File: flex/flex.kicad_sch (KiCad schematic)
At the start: 69 parts, among them J1 Conn_01x04_Female, J2 Conn_01x05_Female, J3 Conn_01x03_Female, J4 Conn_01x06_Female, J5 Conn_01x03_Female, SW10 SW_Push, SW11 SW_Push, SW12 SW_Push, SW15 SW_Push, SW16 SW_Push, SW17 SW_Push, SW20 SW_Push, SW21 SW_Push, SW22 SW_Push, SW24 SW_Push, SW25 SW_Push, SW26 SW_Push, SW6 SW_Push, SW7 SW_Push, SW8 SW_Push

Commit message: licenses
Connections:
- net Gnd: no longer D21.2 (VSS), D22.2 (VSS), D23.2 (VSS), D24.2 (VSS), D25.2 (VSS), D26.2 (VSS), D37.2 (VSS), D38.2 (VSS), D39.2 (VSS), D40.2 (VSS), D41.2 (VSS), D42.2 (VSS), D47.2 (VSS), D48.2 (VSS), D49.2 (VSS), D50.2 (VSS), D51.2 (VSS), D52.2 (VSS), D55.2 (VSS), D56.2 (VSS), D57.2 (VSS), D58.2 (VSS), D59.2 (VSS), D60.2 (VSS)
- net Vcc: no longer D21.4 (VDD), D22.4 (VDD), D23.4 (VDD), D24.4 (VDD), D25.4 (VDD), D26.4 (VDD), D33.4 (VDD), D37.4 (VDD), D38.4 (VDD), D39.4 (VDD), D40.4 (VDD), D41.4 (VDD), D42.4 (VDD), D47.4 (VDD), D48.4 (VDD), D49.4 (VDD), D5.4 (VDD), D50.4 (VDD), D51.4 (VDD), D52.4 (VDD), D55.4 (VDD), D56.4 (VDD), D57.4 (VDD), D58.4 (VDD), D59.4 (VDD), D60.4 (VDD), D7.4 (VDD)
- net at D21.3 (DIN), D22.3 (DIN), D33.1 (DOUT): no longer D34.1 (DOUT)
- net at D42.1 (DOUT), D48.3 (DIN): no longer D41.1 (DOUT), D47.3 (DIN)
- net at D5.3 (DIN), D6.3 (DIN): no longer R1.2, R2.2
- new net: D22.2 (VSS), D24.2 (VSS), D26.2 (VSS), D38.2 (VSS), D40.2 (VSS), D42.2 (VSS)
- new net: D22.4 (VDD), D24.4 (VDD), D26.4 (VDD), D38.4 (VDD), D40.4 (VDD), D42.4 (VDD)
- new net: D21.2 (VSS), D23.2 (VSS), D25.2 (VSS), D37.2 (VSS), D39.2 (VSS), D41.2 (VSS), D47.2 (VSS), D49.2 (VSS), D51.2 (VSS)
- new net: D21.4 (VDD), D23.4 (VDD), D25.4 (VDD), D37.4 (VDD), D39.4 (VDD), D41.4 (VDD)
- new net: D33.4 (VDD), D5.4 (VDD), D7.4 (VDD)
- new net: D48.2 (VSS), D50.2 (VSS), D52.2 (VSS), D56.2 (VSS), D58.2 (VSS), D60.2 (VSS)
- new net: D48.4 (VDD), D50.4 (VDD), D52.4 (VDD), D56.4 (VDD), D58.4 (VDD), D60.4 (VDD)
- new net: D41.1 (DOUT), D47.3 (DIN)
- new net: D47.4 (VDD), D49.4 (VDD), D51.4 (VDD), D55.4 (VDD), D57.4 (VDD), D59.4 (VDD)
- new net: D55.2 (VSS), D57.2 (VSS), D59.2 (VSS)
- new net: R1.2, R2.2
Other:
- note added: "Diodes and switches"
- note added: "MCU connector"
- note added: "RGB"
- note added: "RGB connectors"
- note added: "This work is licensed under a Creative Commons Attribution-NonCommercial-ShareAlike 4.0 International License."
- note added: "Thumb cluster connector"
- company: (none) -> bastard keyboards
- title: (none) -> flex.sch
- moved on the sheet: C1, C2, D11, D12, D13, D14, D15, D16, D17, D19, D20, D21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

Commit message: cleanup schem, reversible r and c
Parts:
- removed C2: C, Capacitor_SMD:C_1206_3216Metric_Pad1.42x1.75mm_HandSolder, symbol Device:C
- removed R2: R, Resistor_SMD:R_1206_3216Metric_Pad1.42x1.75mm_HandSolder, symbol Device:R
- added D1, D10, D28, D3, D30, D44, D46, D54, D62, D64, D66, D68, D70, D72, D74: RIGHT_D, custom:Diode_TH_SOD123, symbol Device:D
- added D18, D2, D29, D4, D43, D45, D53, D61, D63, D65, D67, D69, D71, D73, D75: LEFT_D, custom:Diode_TH_SOD123, symbol Device:D
- C1: value C -> NA_C; footprint Capacitor_SMD:C_1206_3216Metric_Pad1.42x1.75mm_HandSolder -> custom:C_1206_3216Metric_Pad1.33x1.80mm_HandSolder_reversible
- D11, D12, D13, D14, D15, D16, D17, D19, D20, D27, D31, D32, D35, D36, D9: value D -> NA_D
- R1: value R -> NA_R; footprint Resistor_SMD:R_1206_3216Metric_Pad1.42x1.75mm_HandSolder -> custom:R_1206_3216Metric_Pad1.30x1.75mm_HandSolder_reversible
- SW10, SW11, SW12, SW15, SW16, SW17, SW20, SW21, SW22, SW24, SW25, SW26, SW6, SW7, SW8: value SW_Push -> NA_SW_Push
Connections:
- net col2: now also D70.1 (K), D71.1 (K), D72.1 (K), D73.1 (K), D74.1 (K), D75.1 (K)
- net col3: now also D64.1 (K), D65.1 (K), D66.1 (K), D67.1 (K), D68.1 (K), D69.1 (K)
- net col4: now also D46.1 (K), D53.1 (K), D54.1 (K), D61.1 (K), D62.1 (K), D63.1 (K)
- net col5: now also D28.1 (K), D29.1 (K), D30.1 (K), D43.1 (K), D44.1 (K), D45.1 (K)
- net col6: now also D1.1 (K), D10.1 (K), D18.1 (K), D2.1 (K), D3.1 (K), D4.1 (K)
- net at D27.2 (A), SW16.2: now also D54.2 (A), D61.2 (A)
- net at D9.2 (A), SW6.2: now also D70.2 (A), D71.2 (A)
- net at D17.2 (A), SW12.2: now also D68.2 (A), D69.2 (A)
- net at D31.2 (A), SW22.2: now also D44.2 (A), D45.2 (A)
- net at D32.2 (A), SW21.2: now also D30.2 (A), D43.2 (A)
- net at D35.2 (A), SW26.2: now also D10.2 (A), D18.2 (A)
- net at D19.2 (A), SW11.2: now also D66.2 (A), D67.2 (A)
- net at D20.2 (A), SW17.2: now also D62.2 (A), D63.2 (A)
- net at D12.2 (A), SW8.2: now also D74.2 (A), D75.2 (A)
- net at D16.2 (A), SW24.2: now also D1.2 (A), D2.2 (A)
- net at D14.2 (A), SW20.2: now also D28.2 (A), D29.2 (A)
- net at D36.2 (A), SW25.2: now also D3.2 (A), D4.2 (A)
- net at D11.2 (A), SW10.2: now also D64.2 (A), D65.2 (A)
- net at D13.2 (A), SW15.2: now also D46.2 (A), D53.2 (A)
- net at D15.2 (A), SW7.2: now also D72.2 (A), D73.2 (A)
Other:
- moved on the sheet: C1, D11, D12, D13, D14, D15, D16, D17, D19, D20, D21, D22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

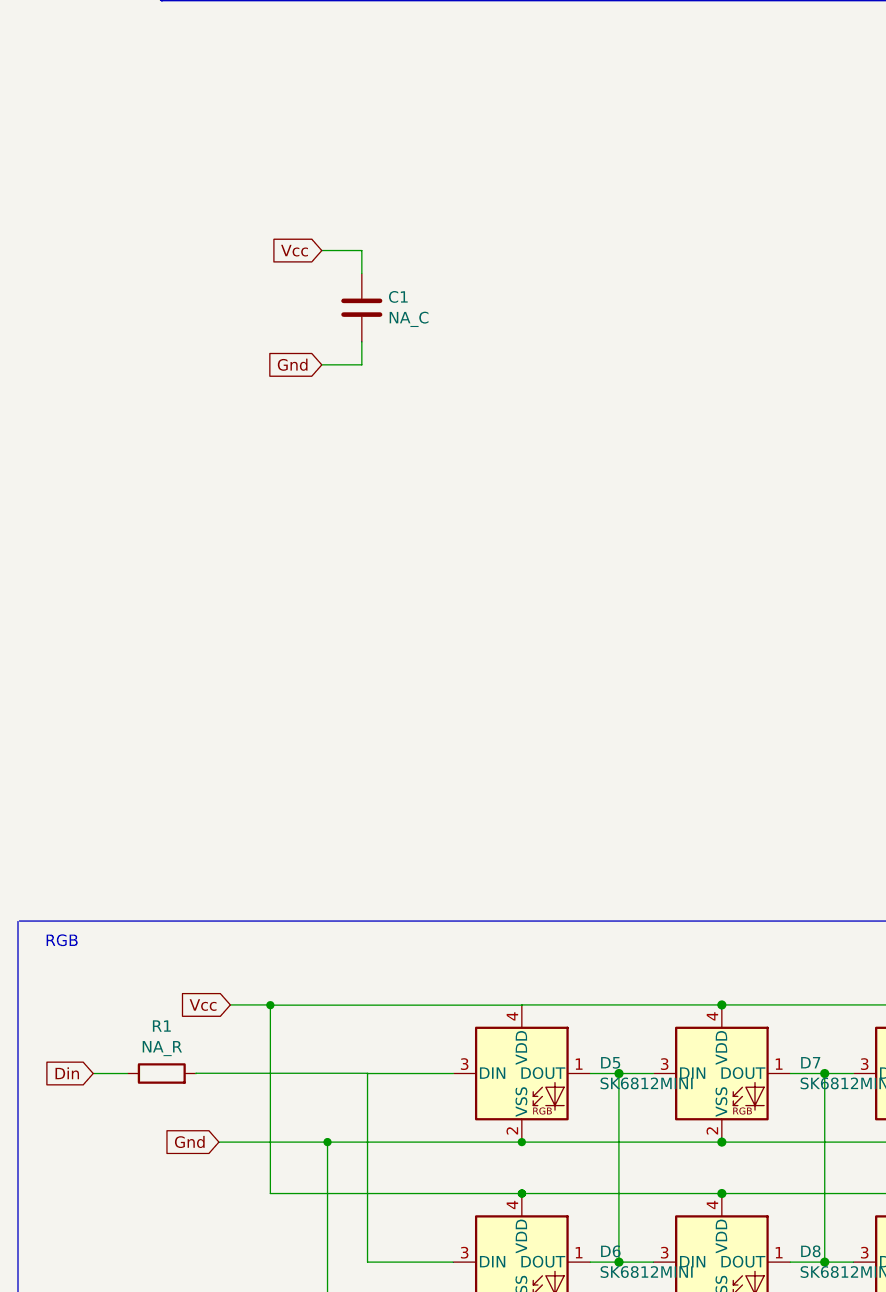
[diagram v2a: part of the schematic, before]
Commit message: place smd components
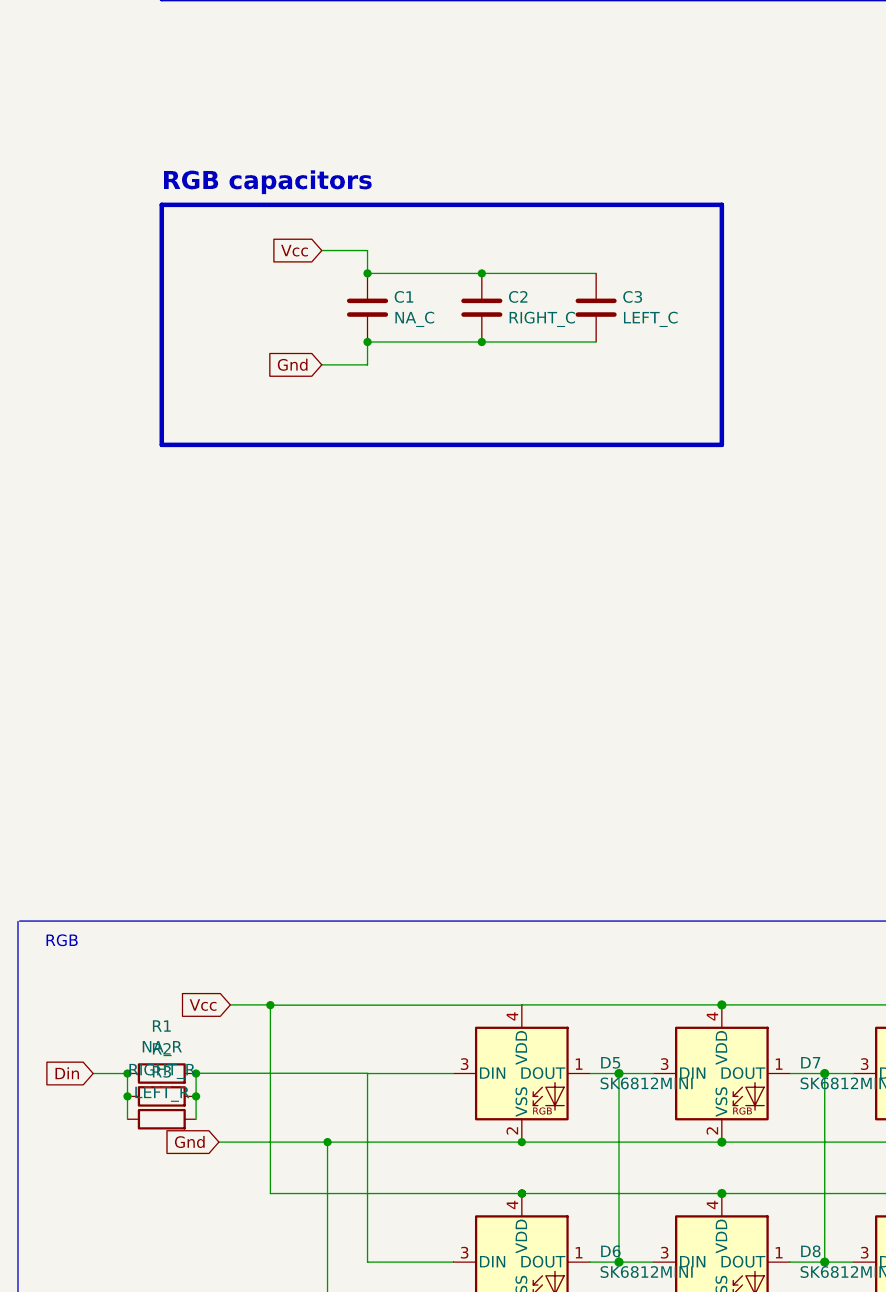
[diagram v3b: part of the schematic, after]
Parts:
- added C2: RIGHT_C, custom:R_0402, symbol Device:C
- added C3: LEFT_C, custom:R_0402, symbol Device:C
- added R2: RIGHT_R, custom:R_0402, symbol Device:R
- added R3: LEFT_R, custom:R_0402, symbol Device:R
- D1, D10, D18, D2, D28, D29, D3, D30, D4, D43, D44, D45, D46, D53, D54, D61, D62, D63, D64, D65, D66, D67, D68, D69, D70, D71, D72, D73, D74, D75: footprint custom:Diode_TH_SOD123 -> custom:D_SOD-523
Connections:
- net Din: now also R2.1, R3.1
- net Gnd: now also C2.2, C3.2
- net Vcc: now also C2.1, C3.1
- net at R1.2: now also R2.2, R3.2
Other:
- note added: "RGB capacitors"
- moved on the sheet: C1

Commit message: change LEDs
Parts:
- D21, D23, D25, D33, D37, D39, D41, D47, D49, D5, D51, D55, D57, D59, D7: value SK6812MINI -> RIGHT_LED; footprint libs2:YS-SK6812MINI-E_REVERSE -> custom:SK6812_mini_e_corners
- D22, D24, D26, D34, D38, D40, D42, D48, D50, D52, D56, D58, D6, D60, D8: value SK6812MINI -> LEFT_LED; footprint libs2:YS-SK6812MINI-E_REVERSE_NO_EDGECUT -> custom:SK6812_mini_e_corners_noedgecuts
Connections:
- net Gnd: now also D21.2 (VSS), D22.2 (VSS), D23.2 (VSS), D24.2 (VSS), D25.2 (VSS), D26.2 (VSS), D37.2 (VSS), D38.2 (VSS), D39.2 (VSS), D40.2 (VSS), D41.2 (VSS), D42.2 (VSS), D47.2 (VSS), D48.2 (VSS), D49.2 (VSS), D50.2 (VSS), D51.2 (VSS), D52.2 (VSS), D55.2 (VSS), D56.2 (VSS), D57.2 (VSS), D58.2 (VSS), D59.2 (VSS), D60.2 (VSS)
- net Vcc: now also D21.4 (VDD), D22.4 (VDD), D23.4 (VDD), D24.4 (VDD), D25.4 (VDD), D26.4 (VDD), D33.4 (VDD), D37.4 (VDD), D38.4 (VDD), D39.4 (VDD), D40.4 (VDD), D41.4 (VDD), D42.4 (VDD), D47.4 (VDD), D48.4 (VDD), D49.4 (VDD), D5.4 (VDD), D50.4 (VDD), D51.4 (VDD), D52.4 (VDD), D55.4 (VDD), D56.4 (VDD), D57.4 (VDD), D58.4 (VDD), D59.4 (VDD), D60.4 (VDD), D7.4 (VDD)
- net at D21.3 (DIN), D22.3 (DIN), D33.1 (DOUT): now also D34.1 (DOUT)
- net at D5.3 (DIN), D6.3 (DIN): now also R1.2, R2.2, R3.2
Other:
- moved on the sheet: D21, D22, D24, D25, D26, D33, D34, D38, D39, D40, D42, D48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

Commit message: routing
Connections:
- net at D42.1 (DOUT), D48.3 (DIN): now also D41.1 (DOUT), D47.3 (DIN)
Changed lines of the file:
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@@
   (junction (at 247.65 204.47) (diameter 0) (color 0 0 0 0)
+  )
+  (junction (at 259.08 196.85) (diameter 0) (color 0 0 0 0)
   )
   (junction (at 25.4 175.26) (diameter 0) (color 0 0 0 0)
@@
     (stroke (width 0) (type default))
   )
-  (wire (pts (xy 259.08 195.58) (xy 259.08 175.26))
+  (wire (pts (xy 259.08 175.26) (xy 259.08 196.85))
     (stroke (width 0) (type default))
   )
@@
     (stroke (width 0) (type default))
   )
+  (wire (pts (xy 259.08 196.85) (xy 261.62 196.85))
+    (stroke (width 0) (type solid))
+  )
   (wire (pts (xy 55.88 20.32) (xy 55.88 45.72))
     (stroke (width 0) (type default))
@@
     (stroke (width 0) (type solid))
   )
-  (wire (pts (xy 255.27 196.85) (xy 261.62 196.85))
-    (stroke (width 0) (type solid))
-  )
+  (wire (pts (xy 255.27 196.85) (xy 259.08 196.85))
+    (stroke (width 0) (type solid))
+  )

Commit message: bom
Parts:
- J1: value Conn_01x04_Female -> NA_Conn_01x04_Female
- J2: value Conn_01x05_Female -> NA_Conn_01x05_Female
- J3, J5: value Conn_01x03_Female -> NA_Conn_01x03_Female
- J4: value Conn_01x06_Female -> NA_Conn_01x06_Female
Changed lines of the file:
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@@
       (effects (font (size 1.27 1.27)) (justify left))
     )
-    (property "Value" "Conn_01x03_Female" (at 350.2152 95.8342 0)
+    (property "Value" "NA_Conn_01x03_Female" (at 350.2152 95.8342 0)
       (effects (font (size 1.27 1.27)) (justify left))
     )
@@
       (effects (font (size 1.27 1.27)) (justify left))
     )
-    (property "Value" "Conn_01x03_Female" (at 349.8342 107.3658 0)
+    (property "Value" "NA_Conn_01x03_Female" (at 349.8342 107.3658 0)
       (effects (font (size 1.27 1.27)) (justify left))
     )
@@
       (effects (font (size 1.27 1.27)) (justify left))
     )
-    (property "Value" "Conn_01x05_Female" (at 351.536 54.0004 0)
+    (property "Value" "NA_Conn_01x05_Female" (at 351.536 54.0004 0)
       (effects (font (size 1.27 1.27)) (justify left))
     )
@@
       (effects (font (size 1.27 1.27)) (justify left))
     )
-    (property "Value" "Conn_01x04_Female" (at 349.6565 28.2765 0)
+    (property "Value" "NA_Conn_01x04_Female" (at 349.6565 28.2765 0)
       (effects (font (size 1.27 1.27)) (justify left))
     )
@@
       (effects (font (size 1.27 1.27)) (justify left))
     )
-    (property "Value" "Conn_01x06_Female" (at 351.536 70.5104 0)
-      (effects (font (size 1.27 1.27)) (justify left))
-    )
+    (property "Value" "NA_Conn_01x06_Female" (at 351.536 70.5104 0)
+      (effects (font (size 1.27 1.27)) (justify left))
+    )

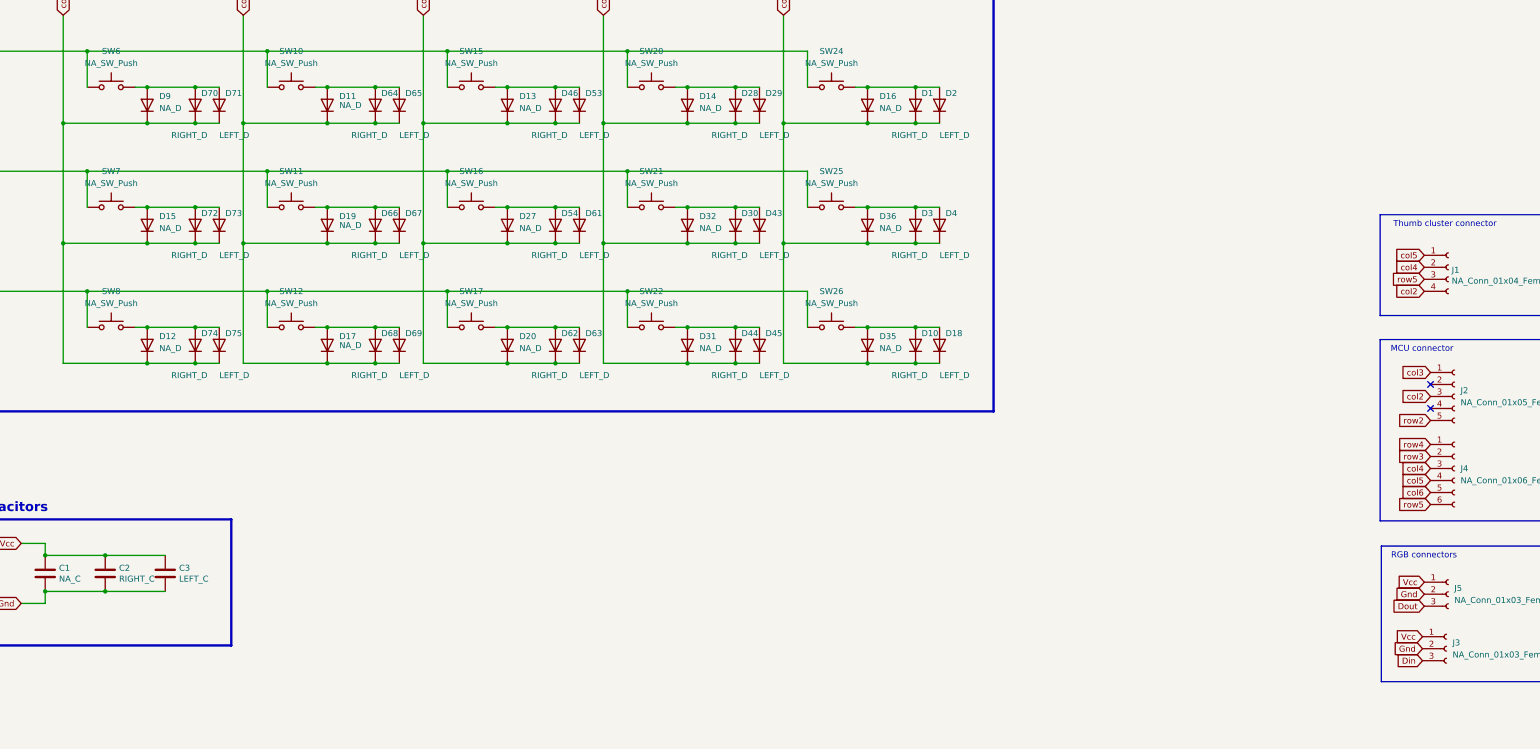
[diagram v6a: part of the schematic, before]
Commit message: remove small diodes
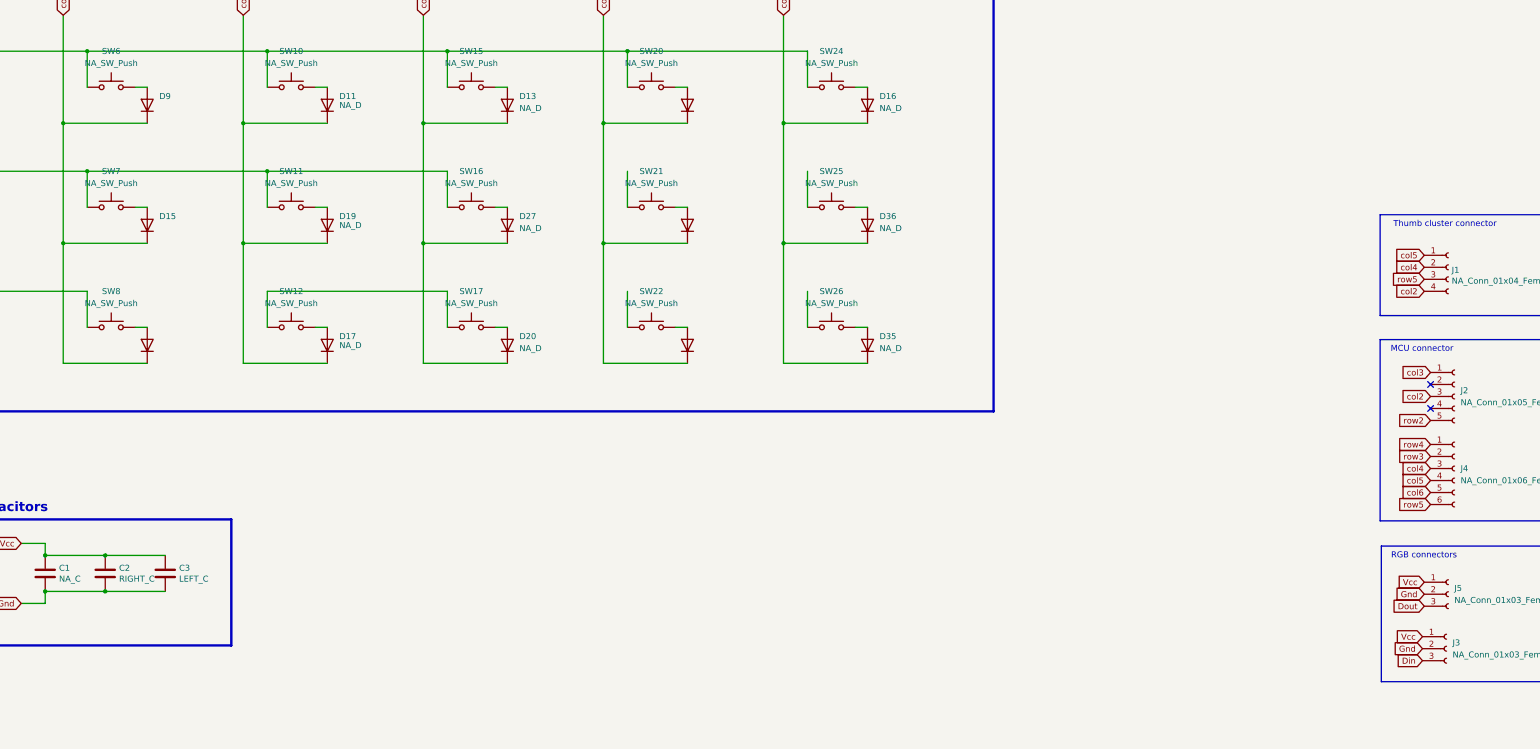
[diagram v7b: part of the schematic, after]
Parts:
- removed D1, D10, D28, D3, D30, D44, D46, D54, D62, D64, D66, D68, D70, D72, D74: RIGHT_D, custom:D_SOD-523, symbol Device:D
- removed D18, D2, D29, D4, D43, D45, D53, D61, D63, D65, D67, D69, D71, D73, D75: LEFT_D, custom:D_SOD-523, symbol Device:D
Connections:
- net row3: no longer SW21.1, SW25.1
- net row4: no longer SW12.1, SW17.1, SW22.1, SW26.1
- new net: SW12.1, SW17.1
